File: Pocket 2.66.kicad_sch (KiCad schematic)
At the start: 87 parts, among them P1 USB-TYPE-C-018, P3 FPC-05F-24PH20, P4 HX-1.25-2AWB, Q1 HL2300, Q2 HL2305, SW1 TS-24CA-S16, SW2 TS-24CA-S16, SW3 TS-24CA-S16, U1 ESP32-C3FH4, U2 LCK-TF-027H30008-WLG, U3 GX4054, U4 GS2019-33TR5, U5 STC3115AIQT, U6 ESD-USB, X1 40MHz 9pF 2016

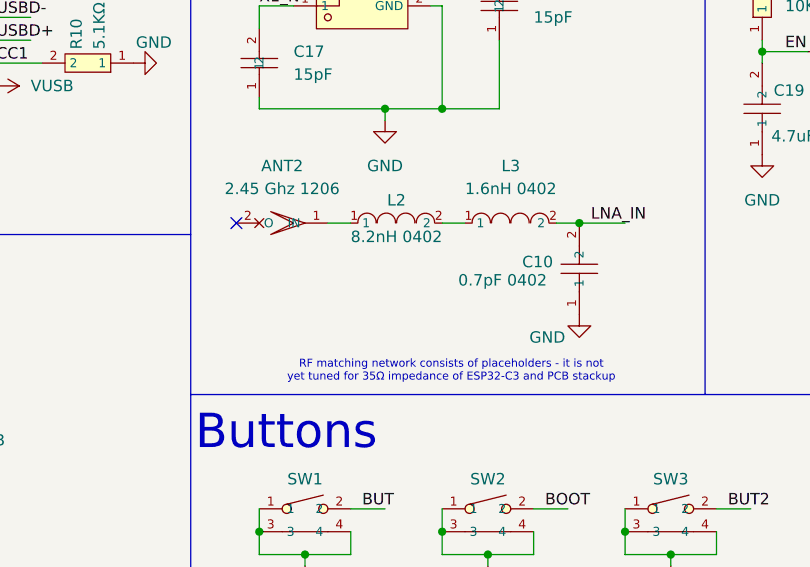
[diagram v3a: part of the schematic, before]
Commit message: Add second RF shunt (DNP) for extra matching flexibility
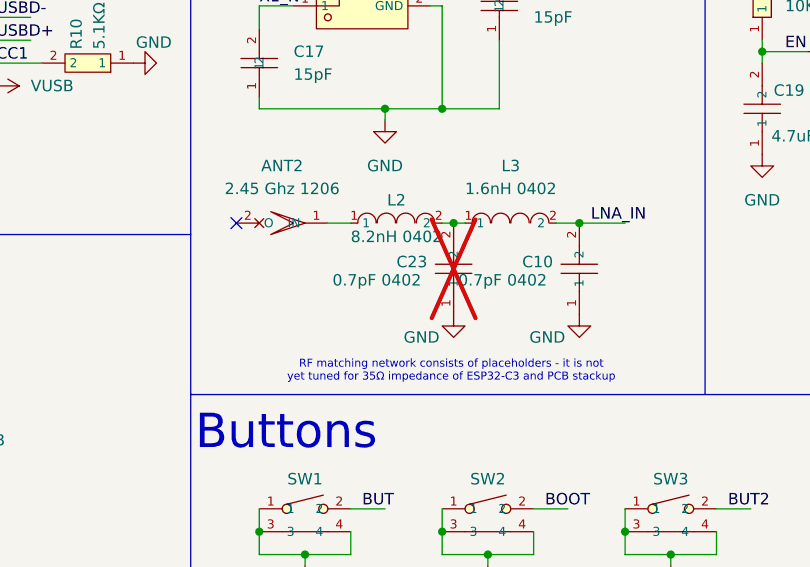
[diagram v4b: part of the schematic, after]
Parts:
- added C23: 0.7pF 0402, LCSC:C0402, symbol LCSC Global:0.7pF 0402
- C30, C31, C9, R3: now left out of the parts list
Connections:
- net GND: now also C23.1
- net at L2.2, L3.1: now also C23.2
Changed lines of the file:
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@@
 	)
 	(junction
+		(at 115.57 60.96)
+		(diameter 0)
+		(color 0 0 0 0)
+	)
+	(junction
 		(at 187.96 27.94)
 		(diameter 0)
@@
 	(wire
 		(pts
+			(xy 115.57 60.96) (xy 114.3 60.96)
+		)
+		(stroke
+			(width 0)
+			(type default)
+		)
+	)
+	(wire
+		(pts
 			(xy 209.55 48.26) (xy 215.9 48.26)
 		)
@@
 	(wire
 		(pts
-			(xy 116.84 60.96) (xy 114.3 60.96)
+			(xy 116.84 60.96) (xy 115.57 60.96)
 		)
 		(stroke
@@
 	)
 	(symbol
+		(lib_id "LCSC Global:0.7pF 0402")
+		(at 115.57 66.04 0)
+		(unit 1)
+		(body_style 1)
+		(exclude_from_sim no)
+		(in_bom no)
+		(on_board yes)
+		(in_pos_files yes)
+		(dnp yes)
+		(property "Reference" "C23"
+			(at 109.22 65.278 0)
+			(show_name no)
+			(do_not_autoplace no)
+			(effects
+				(font
+					(size 1.27 1.27)
+				)
+				(justify left)
+			)
+		)
+		(property "Value" "0.7pF 0402"
+			(at 102.108 67.31 0)
+			(show_name no)
+			(do_not_autoplace no)
+			(effects
+				(font
+					(size 1.27 1.27)
+				)
+				(justify left)
+			)
+		)
+		(property "Footprint" "LCSC:C0402"
+			(at 115.57 76.2 0)
+			(hide yes)
+			(show_name no)
+			(do_not_autoplace no)
+			(effects
+				(font
+					(size 1.27 1.27)
+				)
+			)
+		)
+		(property "Datasheet" "https://wmsc.lcsc.com/wmsc/upload/file/pdf/v2/lcsc/1912111437_Murata-Electronics-GJM1555C1HR70WB01D_C397301.pdf"
+			(at 113.284 65.913 0)
+			(hide yes)
+			(show_name no)
+			(do_not_autoplace no)
+			(effects
+				(font
+					(size 1.27 1.27)
+				)
+			)
+		)
+		(property "Description" "GJM1555C1HR70WB01D"
+			(at 115.57 66.04 0)
+			(hide yes)
+			(show_name no)
+			(do_not_autoplace no)
+			(effects
+				(font
+					(size 1.27 1.27)
+				)
+			)
+		)
+		(property "LCSC" "C397301"
+			(at 115.57 66.04 0)
+			(hide yes)
+			(show_name no)
+			(do_not_autoplace no)
+			(effects
+				(font
+					(size 1.27 1.27)
+				)
+			)
+		)
+		(property "Manufacturer" "muRata"
+			(at 115.57 66.04 0)
+			(hide yes)
+			(show_name no)
+			(do_not_autoplace no)
+			(effects
+				(font
+					(size 1.27 1.27)
+				)
+			)
+		)
+		(property "JLC Type" "Extended"
+			(at 115.57 66.04 0)
+			(hide yes)
+			(show_name no)
+			(do_not_autoplace no)
+			(effects
+				(font
+					(size 1.27 1.27)
+				)
+			)
+		)
+		(property "MPN" "GJM1555C1HR70WB01D"
+			(at 115.57 66.04 0)
+			(hide yes)
+			(show_name no)
+			(do_not_autoplace no)
+			(effects
+				(font
+					(size 1.27 1.27)
+				)
+			)
+		)
+		(property "LCSC Type" ""
+			(at 115.57 66.04 0)
+			(hide yes)
+			(show_name no)
+			(do_not_autoplace no)
+			(effects
+				(font
+					(size 1.27 1.27)
+				)
+			)
+		)
+		(pin "1"
+		)
+		(pin "2"
+		)
+		(instances
+			(project "Pocket 2.66"
+				(path "/1cd4c3f1-5659-46dd-b7c5-63c53cd89f06"
+					(reference "C23")
+					(unit 1)
+				)
+			)
+		)
+	)
+	(symbol
 		(lib_id "power:GND")
 		(at 24.13 85.09 270)
@@
 		(body_style 1)
 		(exclude_from_sim no)
-		(in_bom yes)
+		(in_bom no)
 		(on_board yes)
 		(in_pos_files yes)
@@
 		(body_style 1)
 		(exclude_from_sim no)
-		(in_bom yes)
+		(in_bom no)
 		(on_board yes)
 		(in_pos_files yes)
@@
 		(body_style 1)
 		(exclude_from_sim no)
-		(in_bom yes)
+		(in_bom no)
 		(on_board yes)
 		(in_pos_files yes)
@@
 	)
 	(symbol
+		(lib_id "power:GND")
+		(at 115.57 71.12 0)
+		(unit 1)
+		(body_style 1)
+		(exclude_from_sim no)
+		(in_bom yes)
+		(on_board yes)
+		(in_pos_files yes)
+		(dnp no)
+		(property "Reference" "#PWR056"
+			(at 115.57 77.47 0)
+			(hide yes)
+			(show_name no)
+			(do_not_autoplace no)
+			(effects
+				(font
+					(size 1.27 1.27)
+				)
+			)
+		)
+		(property "Value" "GND"
+			(at 112.014 73.66 0)
+			(show_name no)
+			(do_not_autoplace no)
+			(effects
+				(font
+					(size 1.27 1.27)
+				)
+			)
+		)
+		(property "Footprint" ""
+			(at 115.57 71.12 0)
+			(hide yes)
+			(show_name no)
+			(do_not_autoplace no)
+			(effects
+				(font
+					(size 1.27 1.27)
+				)
+			)
+		)
+		(property "Datasheet" ""
+			(at 115.57 71.12 0)
+			(hide yes)
+			(show_name no)
+			(do_not_autoplace no)
+			(effects
+				(font
+					(size 1.27 1.27)
+				)
+			)
+		)
+		(property "Description" "Power symbol creates a global label with name \"GND\" , ground"
+			(at 115.57 71.12 0)
+			(hide yes)
+			(show_name no)
+			(do_not_autoplace no)
+			(effects
+				(font
+					(size 1.27 1.27)
+				)
+			)
+		)
+		(pin "1"
+		)
+		(instances
+			(project "Pocket 2.66"
+				(path "/1cd4c3f1-5659-46dd-b7c5-63c53cd89f06"
+					(reference "#PWR056")
+					(unit 1)
+				)
+			)
+		)
+	)
+	(symbol
 		(lib_id "LCSC Global:4.7uF 0402 10V")
 		(at 39.37 161.29 90)
@@
 		(body_style 1)
 		(exclude_from_sim no)
-		(in_bom yes)
+		(in_bom no)
 		(on_board yes)
 		(in_pos_files yes)

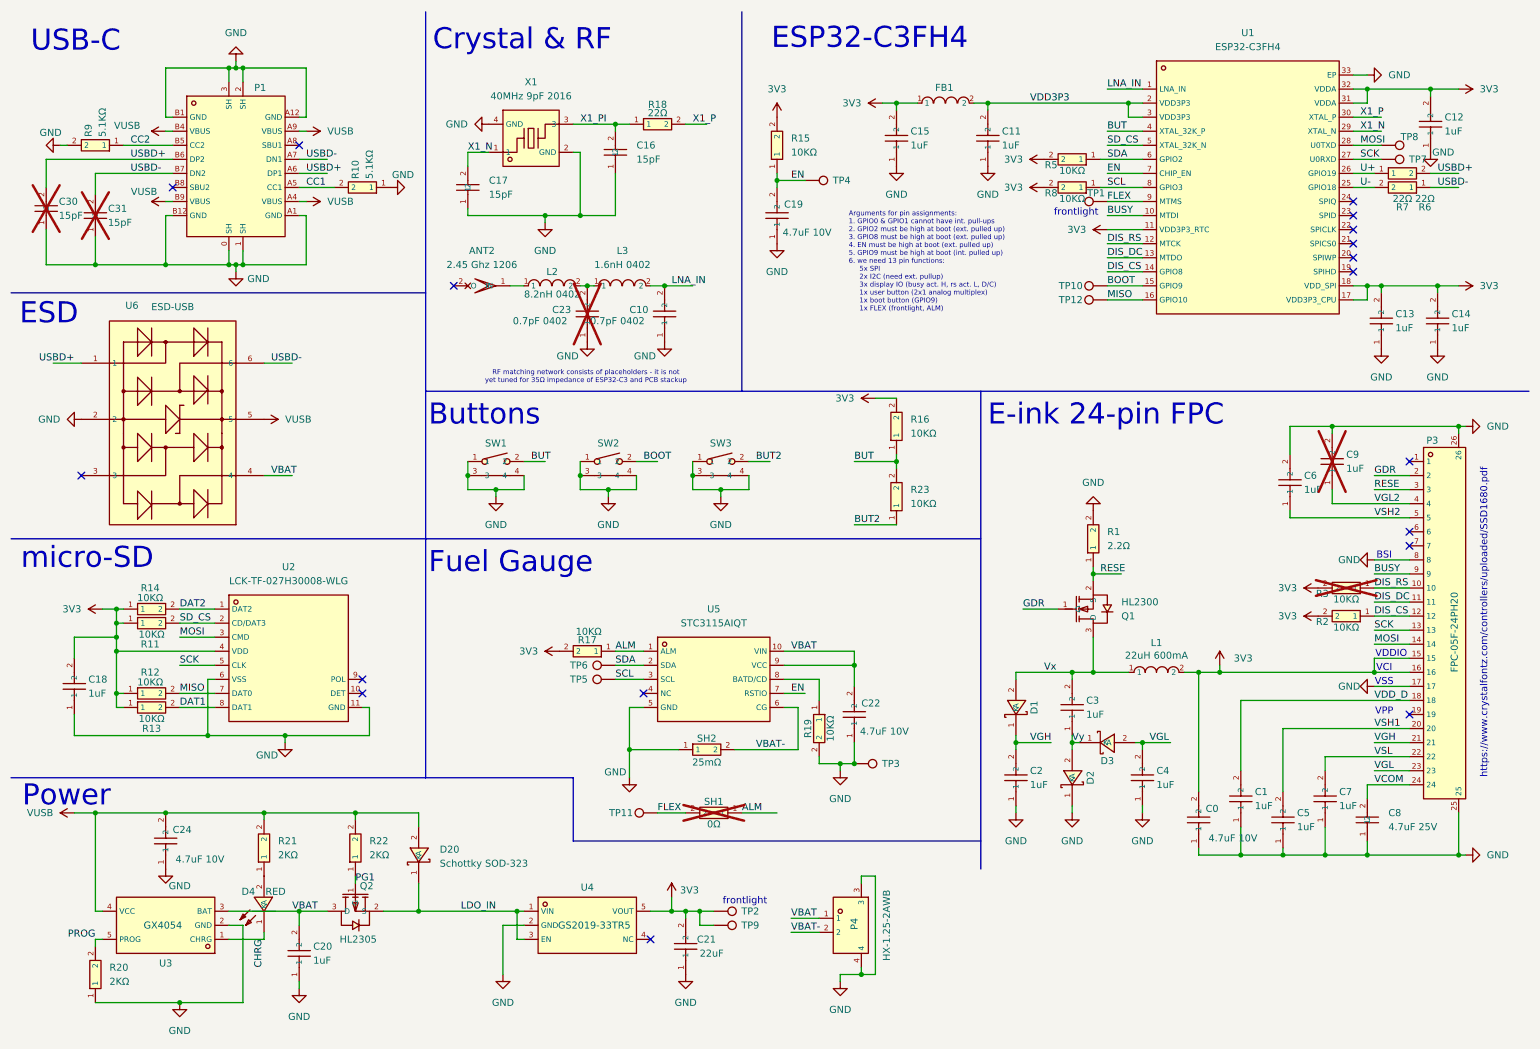
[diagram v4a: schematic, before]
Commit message: Add SD103AWS-L symbol (C41376466) and rename LCSC Type to JLC Type
- New symbol SD103AWS-L SOD-323 (C41376466, PIELENST) with same
  SOD-323 footprint/pinout as C191023, JLC Type: Extended
- Rename all "LCSC Type" properties to "JLC Type" in 5 symbol files
  and 77 occurrences in the schematic
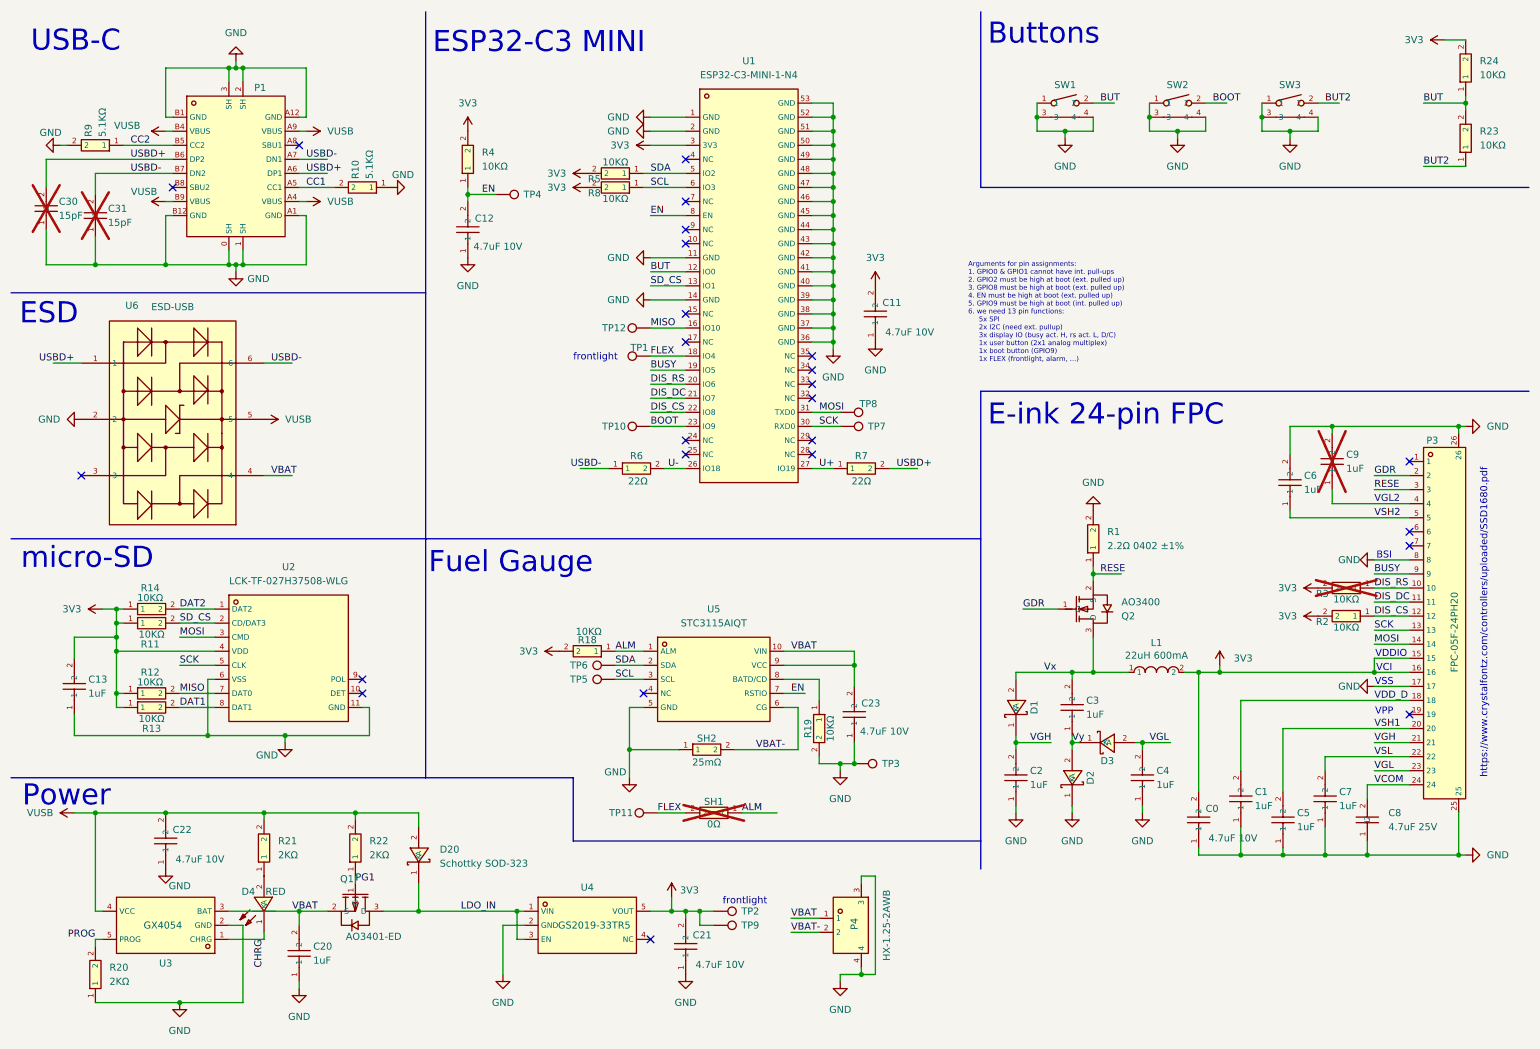
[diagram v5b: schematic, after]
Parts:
- removed ANT2: 2.45 Ghz 1206, LCSC:SMD_ANT_1206, symbol LCSC Global:2.45 GHz SMD antenna
- removed C10, C23: 0.7pF 0402, LCSC:C0402, symbol LCSC Global:0.7pF 0402
- removed C11, C12, C13, C14, C15: 1uF, LCSC:C0402, symbol LCSC Global:1uF 0402 25V
- removed C16, C17: 15pF, LCSC:C0402, symbol LCSC Global:15pF 0402 50V
- removed C21: 22uF, LCSC:C59461_C0603, symbol LCSC Global:22uF 0603 6.3V
- removed FB1: BLM18PG121SN1D_C14709, LCSC:C14709_L0603, symbol LCSC Global:BLM18PG121SN1D_C14709
- removed L2: 8.2nH 0402, LCSC:L0402, symbol LCSC Global:8.2nH 0402
- removed L3: 1.6nH 0402, LCSC:L0402, symbol LCSC Global:1.6nH 0402
- removed Q1: HL2300, LCSC:SOT23-3, symbol LCSC Global:HL2300_C7420343
- removed Q2: HL2305, LCSC:SOT23-3, symbol LCSC Global:HL2305
- removed R1: 2.2Ω, LCSC:R0603, symbol LCSC Global:2.2Ω 0603 ±1%
- removed R18, R6, R7: 22Ω, LCSC:R0402, symbol LCSC Global:22Ω 0402 ±1%
- removed U1: ESP32-C3FH4, LCSC:C2858491_QFN-32_L5_0-W5_0-P0_50-TL-EP3_7, symbol LCSC Global:ESP32-C3FH4
- removed U2: LCK-TF-027H30008-WLG, LCSC:C50380692_TF-SMD_HYCW104-TF08-375B, symbol LCSC Global:LCK-TF-027H30008-WLG
- removed X1: 40MHz 9pF 2016, LCSC:C49304717_CRYSTAL-SMD_4P-L2_0-W1_6-BL, symbol LCSC Global:40MHz 9pF SMD2016
- added C11, C21: 4.7uF 10V, LCSC:C0402, symbol LCSC Global:4.7uF 0402 10V
- added Q1: AO3401-ED, LCSC:SOT23-3, symbol LCSC Global:AO3401-ED
- added Q2: AO3400, LCSC:SOT-23-L, symbol LCSC Global:AO3400
- added R1: 2.2Ω 0402 ±1%, LCSC:R0402, symbol LCSC Global:2.2Ω 0402 ±1%
- added R6, R7: 22Ω, LCSC:R0402, symbol LCSC Global:22Ω 0402 ±1% (Yageo)
- added U1: ESP32-C3-MINI-1-N4, LCSC:C2838502_WIFIM-SMD_ESP32-C3-MINI-1, symbol LCSC Global:ESP32-C3-MINI-1-N4
- added U2: LCK-TF-027H37508-WLG, LCSC:C50380692_TF-SMD_HYCW104-TF08-375B, symbol LCSC Global:LCK-TF-027H37508-WLG
- D4: JLC Type Basic -> (none)
- P1, P3, P4, SW1, SW2, SW3, U3, U4, U5: JLC Type Extended -> (none)
- U6: JLC Type Promotional -> (none)
- renumbered C19 to C12, C18 to C13, C24 to C22, C22 to C23, R17 to R18, R16 to R24, R15 to R4
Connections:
- net 3V3: now also C11.2, C21.2, U1.3 (3V3), U2.4 (VDD)
- net BOOT: now also U1.23 (IO9)
- net BUSY: now also U1.19 (IO5)
- net BUT: now also U1.12 (IO0)
- net DAT1: now also U2.8 (DAT1)
- net DAT2: now also U2.1 (DAT2)
- net DIS_CS: now also U1.22 (IO8)
- net DIS_DC: now also U1.21 (IO7)
- net DIS_RS: now also U1.20 (IO6)
- net EN: now also U1.8 (EN)
- net FLEX: now also U1.18 (IO4)
- net GDR: now also Q2.1 (G)
- net GND: now also C11.1, C21.1, R1.2, U1.1 (GND), U1.11 (GND), U1.14 (GND), U1.2 (GND), U1.36 (GND), U1.37 (GND), U1.38 (GND), U1.39 (GND), U1.40 (GND), U1.41 (GND), U1.42 (GND), U1.43 (GND), U1.44 (GND), U1.45 (GND), U1.46 (GND), U1.47 (GND), U1.48 (GND), U1.49 (GND), U1.50 (GND), U1.51 (GND), U1.52 (GND), U1.53 (GND), U2.11 (GND), U2.6 (VSS)
- net LDO_IN: now also Q1.3 (D)
- net MISO: now also U1.16 (IO10), U2.7 (DAT0)
- net MOSI: now also U1.31 (TXD0), U2.3 (CMD)
- net PG1: now also Q1.1 (G)
- net RESE: now also Q2.2 (S), R1.1
- net SCK: now also U1.30 (RXD0), U2.5 (CLK)
- net SCL: now also U1.6 (IO3)
- net SDA: now also U1.5 (IO2)
- net SD_CS: now also U1.13 (IO1), U2.2 (CD/DAT3)
- net U+: now also R7.1, U1.27 (IO19)
- net U-: now also R6.2, U1.26 (IO18)
- net USBD+: now also R7.2
- net USBD-: now also R6.1
- net VBAT: now also Q1.2 (S)
- net Vx: now also Q2.3 (D)
- no-connect marks 18 -> 25
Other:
- note added: "ESP32-C3 MINI"
- note removed: "Crystal & RF"
- note removed: "ESP32-C3FH4"
- note removed: "RF matching network consists of placeholders - it is not yet tuned for 35Ω impedance of ESP32-C3 and PCB stackup"
- moved on the sheet: C12, R23, R24, R4, SW1, SW2, SW3, TP4

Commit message: Schematics for ESP32-C3 mini module
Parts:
- removed C0, C11, C12, C21, C22, C23: 4.7uF 10V, LCSC:C0402, symbol LCSC Global:4.7uF 0402 10V
- removed C1, C13, C2, C20, C3, C4, C5, C6, C7, C9: 1uF, LCSC:C0402, symbol LCSC Global:1uF 0402 25V
- removed C8: 4.7uF 25V, LCSC:C1779_C0805, symbol LCSC Global:4.7uF 0805 25V
- removed D1, D2, D20, D3: Schottky SOD-323, LCSC:C191023_SOD-323_L1_8-W1_3-LS2_5-RD, symbol LCSC Global:Schottky SOD-323
- removed R11, R12, R13, R14, R18, R19, R2, R23, R24, R3, R4, R5, R8: 10KΩ, LCSC:R0402, symbol LCSC Global:10KΩ 0402 ±1%
- added C0, C1, C11, C12, C13, C2, C20, C21, C22, C23, C3, C4, C5, C6, C7, C8, C9: 4.7uF, LCSC:C0402, symbol LCSC Global:4.7uF 0402 25V (Non-basic)
- added D1, D2, D20, D3: SD103AWS-L SOD-323, LCSC:C191023_SOD-323_L1_8-W1_3-LS2_5-RD, symbol LCSC Global:SD103AWS-L SOD-323
- added R11, R12, R13, R14, R18, R19, R2, R3, R4: 47kΩ, LCSC:R0402, symbol LCSC Global:47kΩ 0402 ±1%
- added R23, R24, R5, R8: 5.1KΩ, LCSC:R0402, symbol LCSC Global:5.1KΩ 0402 ±1%
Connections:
- net 3V3: now also C0.2, C11.2, C13.2, C21.2, R11.1, R12.1, R13.1, R14.1, R18.2, R2.1, R24.2, R3.1, R4.2, R5.2, R8.1
- net ALM: now also R18.1
- net BUT: now also R23.2, R24.1
- net BUT2: now also R23.1
- net DAT1: now also R11.2
- net DAT2: now also R14.2
- net DIS_CS: now also R2.2
- net DIS_RS: now also R3.2
- net EN: now also C12.2, R4.1
- net GND: now also C0.1, C1.1, C11.1, C12.1, C13.1, C2.1, C20.1, C21.1, C22.1, C23.1, C4.1, C5.1, C6.2, C7.1, C8.1, C9.2, D2.1 (K), R19.1
- net LDO_IN: now also D20.1 (K)
- net MISO: now also R12.2
- net SCL: now also R8.2
- net SDA: now also R5.1
- net SD_CS: now also R13.2
- net VBAT: now also C20.2, C23.2
- net VCOM: now also C8.2
- net VDD_D: now also C1.2
- net VGH: now also C2.2, D1.1 (K)
- net VGL: now also C4.2, D3.2 (A)
- net VGL2: now also C9.1
- net VSH1: now also C5.2
- net VSH2: now also C6.1
- net VSL: now also C7.2
- net VUSB: now also C22.2, D20.2 (A)
- net Vx: now also C3.2, D1.2 (A)
- net Vy: now also C3.1, D2.2 (A), D3.1 (K)
- net at U5.8 (BATD/CD): now also R19.2
